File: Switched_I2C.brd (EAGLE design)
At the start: 35.2 x 17.4 mm, 15 parts, among them Q1 MOSFET-NCH-DMG3404L

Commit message: Fixed silk screen issues on Switched_I2C board
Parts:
- removed U$4: (no value), awickert:NWLOGO_MED
- added U$9: (no value), awickert:NWLOGO_SMALL
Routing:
- net 3V3: track 88.2 -> 98.0 mm
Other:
- board text added: "Project Heptapod Switch ----------- Designed by Northern Widget and University of Minnesota"
- board text removed: "Project Heptapod ----------- Designed by Northern Widget and University of Minnesota"
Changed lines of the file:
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@@
 <hole x="32.512" y="14.859" drill="3.45"/>
 <hole x="2.667" y="14.859" drill="3.45"/>
-<text x="30.48" y="6.604" size="0.8128" layer="52" font="vector" ratio="15" distance="40" rot="MR0" align="center-left">Project Heptapod
+<text x="30.48" y="7.112" size="0.8128" layer="52" font="vector" ratio="15" distance="40" rot="MR0" align="center-left">Project Heptapod
+Switch
 -----------
 Designed by
@@
 <element name="U$6" library="bschulz" package="1X04" value="CONN_4SCREW_2.54" x="23.114" y="14.097"/>
 <element name="U$7" library="bschulz" package="1X04" value="CONN_4SCREW_2.54" x="31.877" y="5.334" rot="R270"/>
-<element name="U$4" library="awickert" package="NWLOGO_MED" value="" x="27.94" y="-3.81" rot="MR0"/>
 <element name="U$5" library="bschulz" package="TSSOP16" value="SN74LV4051ATSSOP" x="8.89" y="9.398" rot="MR90">
 <attribute name="DIGIKEY" value="296-41644-1-ND" x="8.89" y="9.398" size="0.8128" layer="28" font="vector" ratio="15" rot="MR90" display="off"/>
@@
 </element>
 <element name="Q1" library="bschulz" package="SOT23-3" value="MOSFET-NCH-DMG3404L" x="25.019" y="2.159" rot="MR0"/>
+<element name="U$9" library="awickert" package="NWLOGO_SMALL" value="" x="29.21" y="2.54" rot="MR0"/>
 </elements>
 <signals>
@@
 <wire x1="8.255" y1="1.3716" x2="9.2964" y2="1.3716" width="0.254" layer="1"/>
 <wire x1="9.2964" y1="1.3716" x2="9.398" y2="1.27" width="0.254" layer="1"/>
-<wire x1="9.398" y1="3.7846" x2="11.8078" y2="7.123" width="0" layer="19" extent="1-16"/>
+<wire x1="6.58323125" y1="6.6912" x2="5.9292" y2="6.6912" width="0.254" layer="16"/>
+<wire x1="5.9292" y1="6.6912" x2="3.302" y2="4.064" width="0.254" layer="16"/>
+<wire x1="11.8078" y1="7.123" x2="7.01503125" y2="7.123" width="0.254" layer="16"/>
+<wire x1="7.01503125" y1="7.123" x2="6.58323125" y2="6.6912" width="0.254" layer="16"/>
 </signal>
 <signal name="GND">

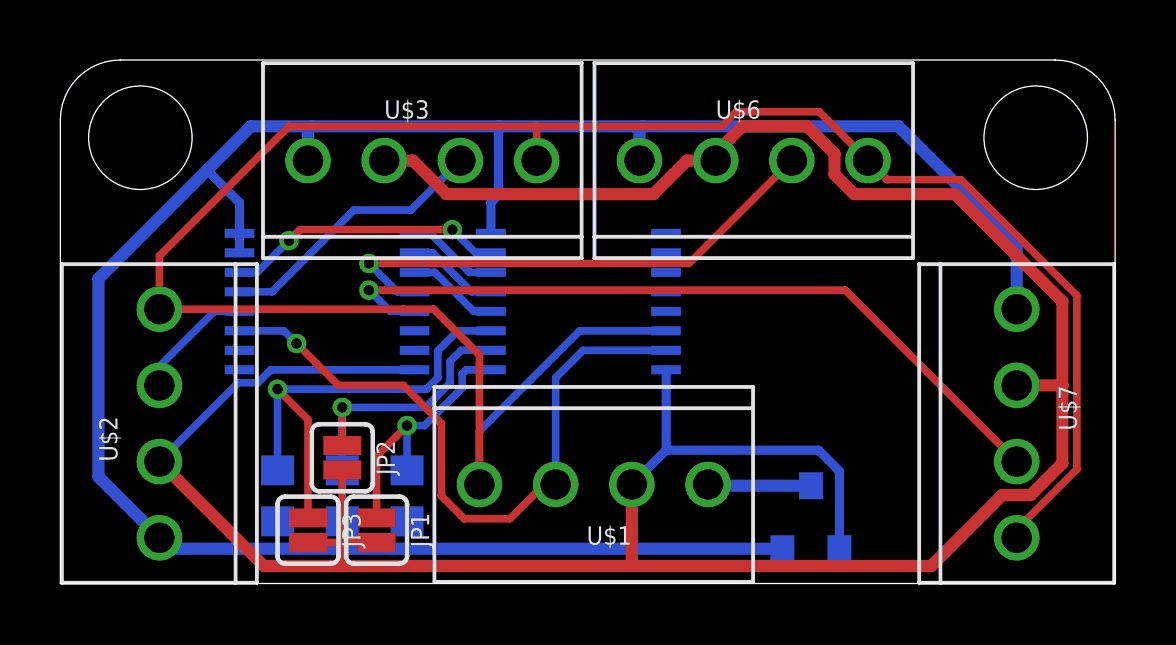
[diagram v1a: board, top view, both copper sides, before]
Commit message: Added RS485 Heptapod
Added RS485 heptapod for use with TP-Downhole Longbow, ready for review before sending out. Also added gerbers for switched and conventional heptapod. Evidently been sitting in buffer for 6 months. Oops.
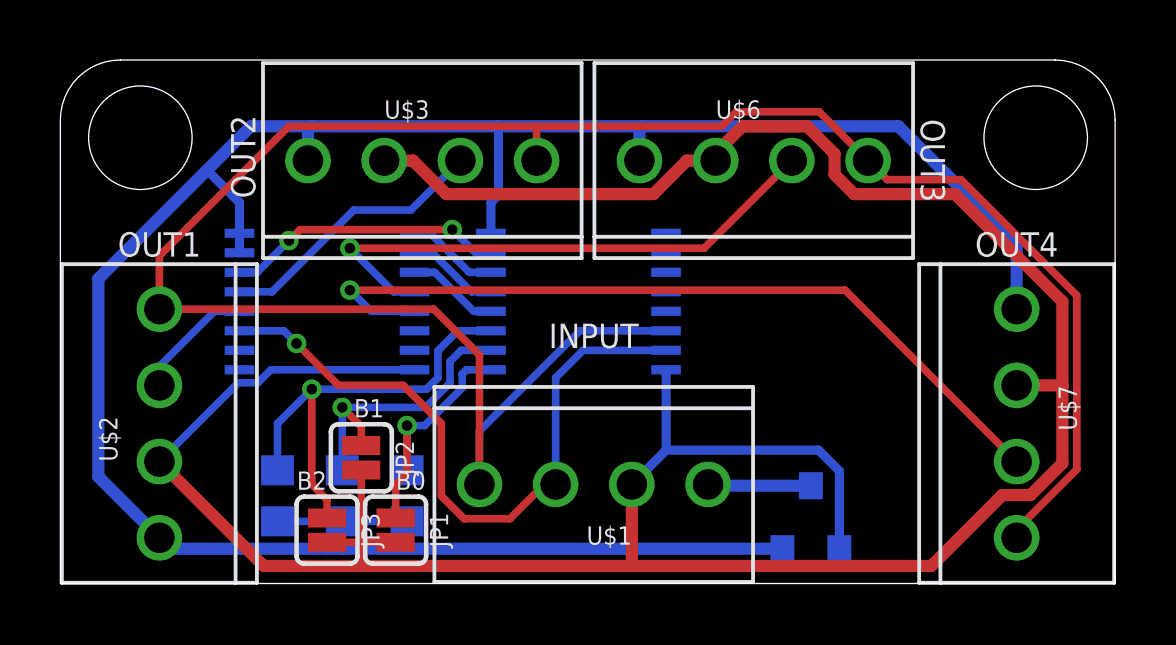
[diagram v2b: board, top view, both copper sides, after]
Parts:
- moved JP1 0.63 mm to (11.2, 1.78)
- moved JP2 0.63 mm to (10.0, 4.19)
- moved JP3 0.63 mm to (8.89, 1.78)
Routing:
- net SDA_3: track 17.4 -> 18.7 mm
- net SDA_4: track 25.8 -> 27.0 mm
- net SEL2: track 15.9 -> 15.0 mm
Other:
- board text added: "B0"
- board text added: "B1"
- board text added: "B2"
- board text added: "INPUT"
- board text added: "OUT1"
- board text added: "OUT2"
- board text added: "OUT3"
- board text added: "OUT4"
